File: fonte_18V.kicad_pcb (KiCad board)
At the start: 2 copper layers, 100 x 52 mm, 35 parts, among them J1 MSTBA, J2 MSTBA, J3 RJ45_Shielded, J4 RJ45_Shielded, Q1 Si2308CDS, U1 LMR16030

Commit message: temp
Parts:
- removed Ci2: 10u, Capacitor_THT:CP_Radial_D5.0mm_P2.50mm
- removed D1: MBR20200CTG, Package_TO_SOT_THT:TO-220-3_Horizontal_TabDown_SMD
- removed F1: 2A, KicadZeniteSolarLibrary18:Fuse_Holder_5x20
- removed J1, J2: MSTBA, Connector_Phoenix_MSTB:PhoenixContact_MSTBA_2,5_2-G-5,08_1x02_P5.08mm_Horizontal
- added Cie101: 10u, Capacitor_THT:CP_Radial_D5.0mm_P2.50mm, F.Cu at (60.5, 176.7)
- added D101: 4v7, Diode_SMD:D_MiniMELF, B.Cu at (47.4, 167.6)
- added D102: MBR340, Diode_SMD:D_SMA_Handsoldering, B.Cu at (93.0, 161.4)
- added D103: B1100, Diode_SMD:D_SMA_Handsoldering, F.Cu at (60.5, 160.0)
- added D104: B1100, Diode_SMD:D_SMA_Handsoldering, F.Cu at (64.0, 160.0)
- added F101: Fuse, KicadZeniteSolarLibrary18:Fuse_Holder_5x20, F.Cu at (36.1, 170.3)
- added J101: IN, TerminalBlock:TerminalBlock_bornier-3_P5.08mm, F.Cu at (32.6, 167.5)
- added J102: Conn_01x02, TerminalBlock:TerminalBlock_bornier-2_P5.08mm, F.Cu at (32.6, 156.7)
- R2: value 100 -> 1k
- moved RLed1 45.9 mm to (133.2, 168.9)
- moved Led1 45.9 mm to (136.0, 169.0)
- moved Co1 20.4 mm to (91.3, 161.6)
- moved L1 18.9 mm to (68.0, 161.3)
- moved Co3 10.8 mm to (73.8, 162.4)
- moved Co4 9.39 mm to (71.4, 162.6)
- moved Co2 9.11 mm to (85.7, 161.5)
- moved R2 0.71 mm to (45.1, 166.9)
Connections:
- net Net-(R2-Pad1) renamed /EN
- Cff1 pad 1: /CAN_18V -> /CAN_18V_DIODE
- Co1 pad 1: /CAN_18V -> /CAN_18V_DIODE
- Co2 pad 1: /CAN_18V -> /CAN_18V_DIODE
- Co3 pad 1: /CAN_18V -> /CAN_18V_DIODE
- Co4 pad 1: /CAN_18V -> /CAN_18V_DIODE
- J3 pad 1: (no net) -> Net-(J4-Pad1)
- J3 pad 2: (no net) -> Net-(J4-Pad2)
- J3 pad 9: GND -> (no net)
- J4 pad 1: (no net) -> Net-(J4-Pad1)
- J4 pad 2: (no net) -> Net-(J4-Pad2)
- J4 pad 9: GND -> (no net)
- L1 pad 2: /CAN_18V -> /CAN_18V_DIODE
- Led1 pad 2: /CAN_18V -> /CAN_18V_DIODE
- Rfbt2 pad 1: /CAN_18V -> /CAN_18V_DIODE
- U1 pad 6: (no net) -> unconnected-(U1-Pad6)
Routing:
- net /CAN_18V: track 108.7 -> 34.6 mm, vias 1 -> 0
- net Net-(CBoot1-Pad1): track 98.6 -> 34.1 mm, vias 1 -> 0
- net /CAN_18V_DIODE: track 0.00 -> 43.1 mm
- net Net-(J4-Pad1): track 0.00 -> 30.4 mm, vias 0 -> 1
- net Net-(J4-Pad2): track 0.00 -> 27.6 mm
- net GND: track 167.3 -> 147.9 mm, vias 4 -> 3
- net Net-(J101-Pad2): track 0.00 -> 9.50 mm
- net Net-(F1-Pad2): track 9.50 -> 0.00 mm
- net Net-(Cie101-Pad1): track 62.8 -> 58.2 mm

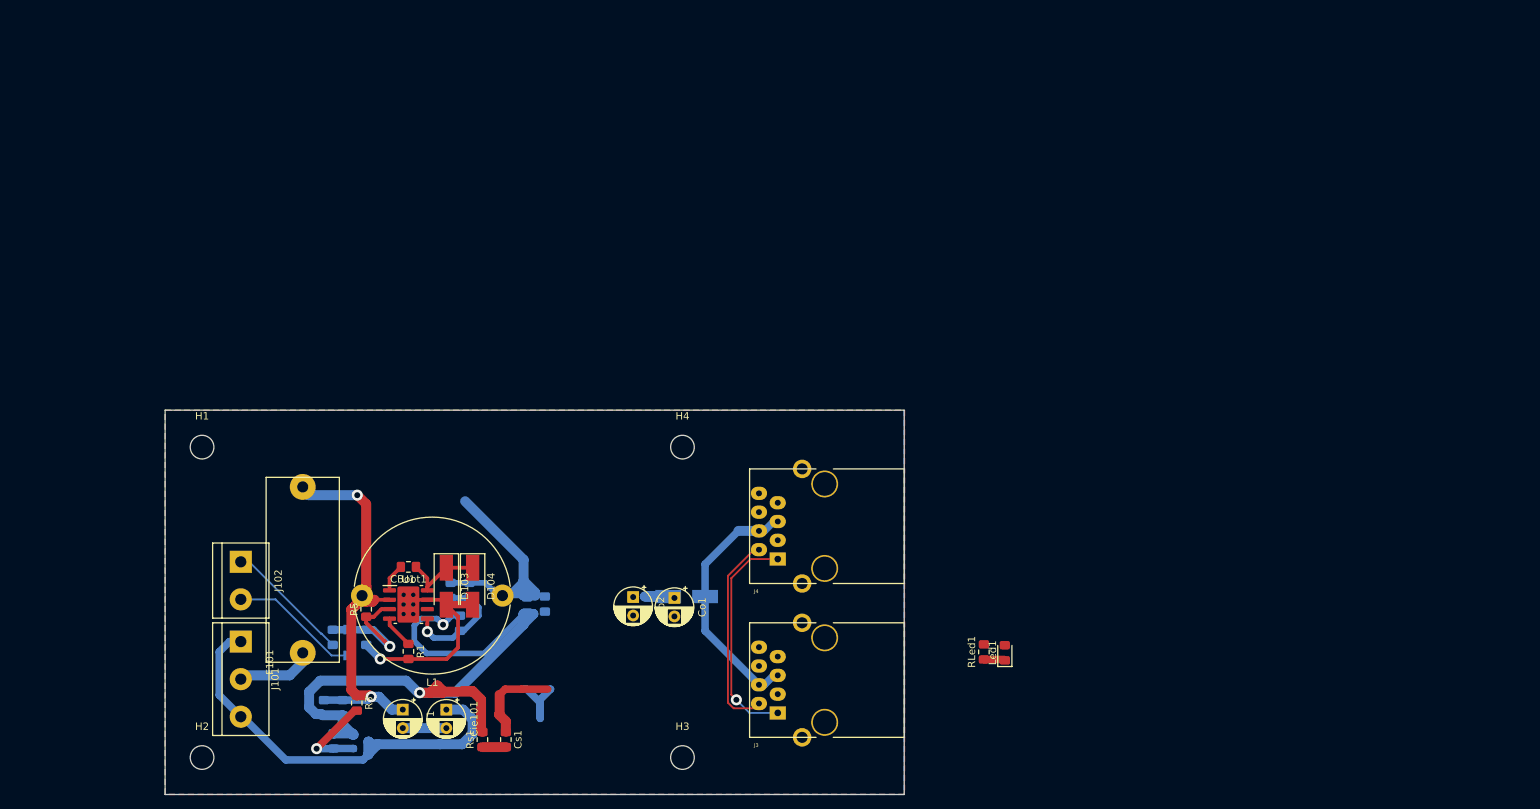
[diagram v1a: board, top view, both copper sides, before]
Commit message: Duplicate fonts for redundancy and initialized layout
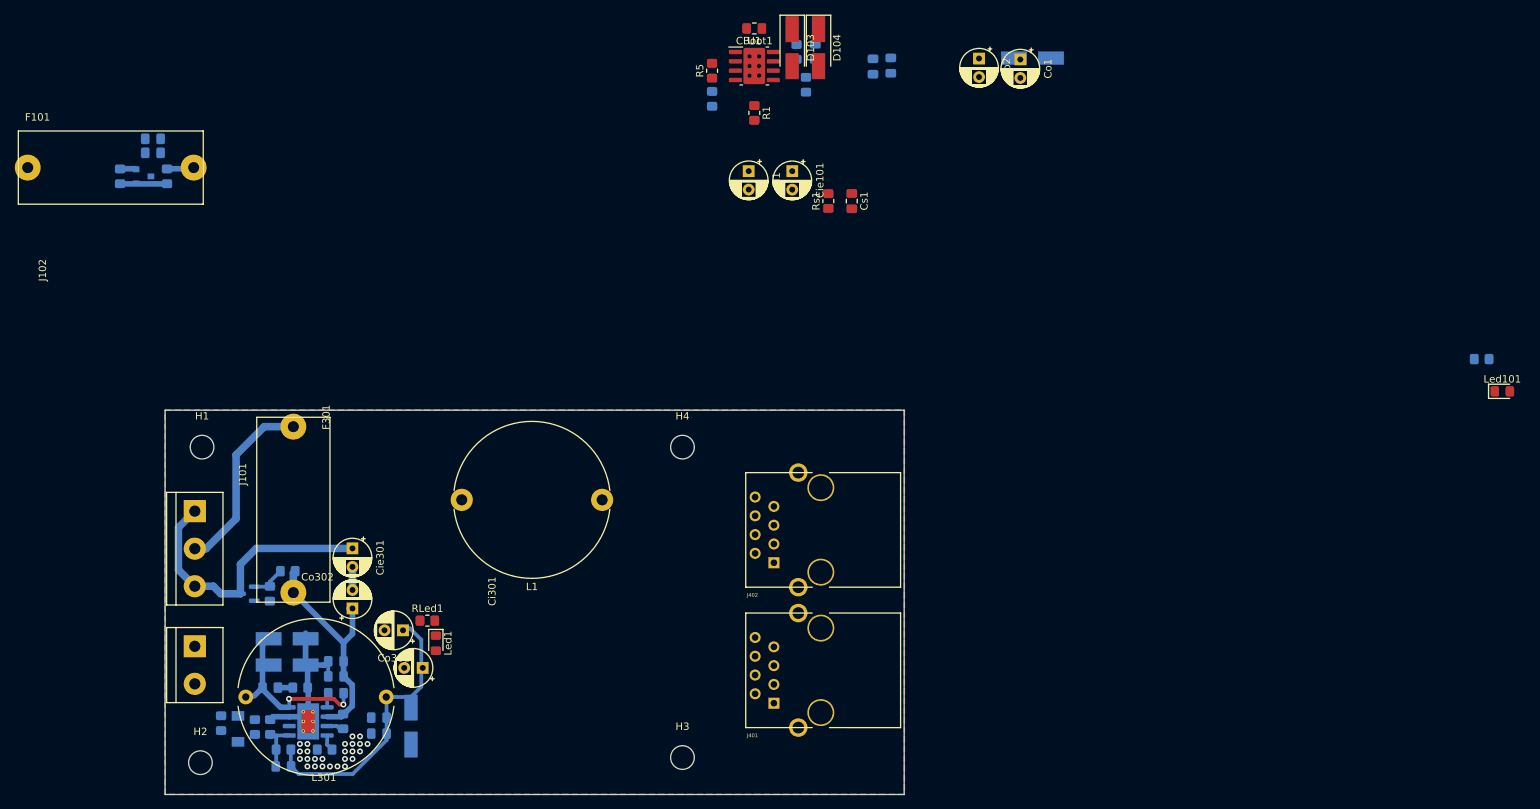
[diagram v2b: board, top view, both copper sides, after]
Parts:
- removed J3, J4: RJ45_Shielded, MFP19RJ45:RJ45_YH59_01
- added CBoot301: 100nF, Capacitor_SMD:C_0805_2012Metric_Pad1.18x1.45mm_HandSolder, B.Cu at (45.5, 174.5)
- added Cff301: na, Capacitor_SMD:C_0805_2012Metric_Pad1.18x1.45mm_HandSolder, B.Cu at (38.4, 184.4)
- added Ci301: 10u, Capacitor_THT:CP_Radial_D5.0mm_P2.50mm, F.Cu at (47.8, 163.0)
- added Cie301: 10u, Capacitor_THT:CP_Radial_D5.0mm_P2.50mm, F.Cu at (47.8, 154.9)
- added Cin301: 100nF, Capacitor_SMD:C_0805_2012Metric_Pad1.18x1.45mm_HandSolder, B.Cu at (45.5, 170.2)
- added Cin302: 100nF, Capacitor_SMD:C_0805_2012Metric_Pad1.18x1.45mm_HandSolder, B.Cu at (45.5, 172.2)
- added Co301: 47u, Capacitor_THT:CP_Radial_D5.0mm_P2.50mm, F.Cu at (54.6, 166.0)
- added Co302: 47u, Capacitor_THT:CP_Radial_D5.0mm_P2.50mm, F.Cu at (57.3, 171.1)
- added Co303: o.1u, Capacitor_SMD:C_0805_2012Metric_Pad1.18x1.45mm_HandSolder, B.Cu at (51.3, 177.8)
- added Co304: 0.1u, Capacitor_SMD:C_0805_2012Metric_Pad1.18x1.45mm_HandSolder, B.Cu at (51.3, 180.0)
- added Cs301: 100n, Capacitor_SMD:C_0805_2012Metric_Pad1.18x1.45mm_HandSolder, B.Cu at (36.6, 173.7)
- added D301: B1100, Diode_SMD:D_SMA_Handsoldering, B.Cu at (38.9, 167.1)
- added D302: B1100, Diode_SMD:D_SMA_Handsoldering, B.Cu at (38.9, 170.7)
- added D303: MBR340, Diode_SMD:D_SMA_Handsoldering, B.Cu at (55.7, 178.9)
- added F301: Fuse, KicadZeniteSolarLibrary18:Fuse_Holder_5x20, F.Cu at (44.7, 137.2)
- added J401: RJ45_Shielded, MFP19RJ45:RJ45_YH59_01, F.Cu at (104.8, 175.8)
- added J402: RJ45_Shielded, MFP19RJ45:RJ45_YH59_01, F.Cu at (104.8, 156.8)
- added L301: 100uH, Inductor_THT:L_Radial_D21.0mm_P19.00mm, F.Cu at (33.3, 175.0)
- added Led101: LED, LED_SMD:LED_0805_2012Metric_Pad1.15x1.40mm_HandSolder, F.Cu at (203.3, 133.6)
- added Q301: Si2308CDS, Package_TO_SOT_SMD:SOT-23, B.Cu at (33.5, 161.0)
- added R301: 220K, Resistor_SMD:R_0805_2012Metric_Pad1.20x1.40mm_HandSolder, B.Cu at (39.0, 158.0)
- added R302: 100K, Resistor_SMD:R_0805_2012Metric_Pad1.20x1.40mm_HandSolder, B.Cu at (36.6, 161.0)
- added R303: 10K, Resistor_SMD:R_0805_2012Metric_Pad1.20x1.40mm_HandSolder, B.Cu at (46.5, 178.3)
- added R304: NA, Resistor_SMD:R_0805_2012Metric_Pad1.20x1.40mm_HandSolder, B.Cu at (34.5, 179.1)
- added R305: 47k, Resistor_SMD:R_0805_2012Metric_Pad1.20x1.40mm_HandSolder, B.Cu at (44.0, 182.1)
- added RLed101: 1k5, Resistor_SMD:R_0805_2012Metric_Pad1.20x1.40mm_HandSolder, B.Cu at (200.5, 129.3)
- added Rfbb301: 8k2, Resistor_SMD:R_0805_2012Metric_Pad1.20x1.40mm_HandSolder, B.Cu at (36.6, 179.1)
- added Rfbt301: 230k, Resistor_SMD:R_0805_2012Metric_Pad1.20x1.40mm_HandSolder, B.Cu at (38.4, 182.1)
- added Rs301: 2k2, Resistor_SMD:R_0805_2012Metric_Pad1.20x1.40mm_HandSolder, B.Cu at (40.7, 173.7)
- added U301: LMR16030, Package_SO:Texas_R-PDSO-G8_EP2.95x4.9mm_Mask2.4x3.1mm_ThermalVias, B.Cu at (41.8, 178.3)
- CBoot1, Cff1, Cin2, Cin3, Co3, Co4, Cs1: footprint Capacitor_SMD:C_0805_2012Metric_Pad1.15x1.40mm_HandSolder -> Capacitor_SMD:C_0805_2012Metric_Pad1.18x1.45mm_HandSolder
- R1, R2, R4, R5, R6, RLed1, Rfbb1, Rfbt2, Rs1: footprint Resistor_SMD:R_0805_2012Metric_Pad1.15x1.40mm_HandSolder -> Resistor_SMD:R_0805_2012Metric_Pad1.20x1.40mm_HandSolder
- R3: footprint Resistor_SMD:R_0805_2012Metric_Pad1.15x1.40mm_HandSolder -> Resistor_SMD:R_0805_2012Metric_Pad1.20x1.40mm_HandSolder; moved to B.Cu
- moved Cff1 86.6 mm to (110.4, 87.7)
- moved Ci1 86.6 mm to (101.4, 103.9)
- moved Cie101 86.6 mm to (107.3, 103.9)
- moved Co1 86.6 mm to (138.1, 88.8)
- moved Co2 86.6 mm to (132.5, 88.6)
- moved Co4 86.6 mm to (118.2, 89.7)
- moved D102 86.6 mm to (139.8, 88.6)
- moved D103 86.6 mm to (107.3, 87.2)
- moved D104 86.6 mm to (110.8, 87.2)
- moved R1 86.6 mm to (102.1, 96.0)
- moved R5 86.6 mm to (96.4, 90.3)
- moved R6 86.6 mm to (96.4, 94.1)
- moved Rfbb1 86.6 mm to (109.1, 92.2)
- moved Rfbt2 86.6 mm to (107.8, 87.7)
- moved U1 86.6 mm to (102.1, 89.6)
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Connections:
- net /Feedback renamed /supply1/Feedback
- net /snbr renamed /supply1/snbr
- net Net-(Cie101-Pad1) renamed /supply1/GND_IN
- net Net-(J101-Pad2) renamed /supply1/IN
- Cff1 pad 1: /CAN_18V_DIODE -> /supply1/CAN_18V_DIODE
- Co1 pad 1: /CAN_18V_DIODE -> /supply1/CAN_18V_DIODE
- Co2 pad 1: /CAN_18V_DIODE -> /supply1/CAN_18V_DIODE
- Co3 pad 1: /CAN_18V_DIODE -> /supply1/CAN_18V_DIODE
- Co4 pad 1: /CAN_18V_DIODE -> /supply1/CAN_18V_DIODE
- D102 pad 1: /CAN_18V -> /CAN/CAN_18V
- D102 pad 2: /CAN_18V_DIODE -> /supply1/CAN_18V_DIODE
- L1 pad 2: /CAN_18V_DIODE -> /supply1/CAN_18V_DIODE
- Led1 pad 2: /CAN_18V_DIODE -> /CAN/CAN_18V
- Rfbt2 pad 1: /CAN_18V_DIODE -> /supply1/CAN_18V_DIODE
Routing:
- net GND: track 147.9 -> 23.7 mm, vias 3 -> 25
- net Net-(Ci1-Pad1): track 61.3 -> 3.45 mm, vias 2 -> 0
- net /CAN_18V_DIODE: track 43.1 -> 0.00 mm
- net /supply2/CAN_18V_DIODE: track 0.00 -> 37.8 mm
- net /CAN_18V: track 34.6 -> 0.00 mm
- net Net-(CBoot1-Pad1): track 34.1 -> 0.00 mm
- net Net-(Ci301-Pad1): track 0.00 -> 31.3 mm
- net Net-(J4-Pad1): track 30.4 -> 0.00 mm, vias 1 -> 0
- net Net-(J4-Pad2): track 27.6 -> 0.00 mm
- net Net-(CBoot301-Pad1): track 0.00 -> 23.6 mm, vias 0 -> 2
- net /supply1/GND_IN: track 58.2 -> 40.1 mm
- net Net-(R2-Pad2): track 17.2 -> 0.00 mm
- net /supply1/Feedback: track 15.8 -> 0.00 mm, vias 1 -> 0
- net /supply1/IN: track 9.50 -> 25.2 mm
- net /EN: track 16.9 -> 2.31 mm, vias 1 -> 0
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
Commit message: almost finished
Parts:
- added D201: MBR340, Diode_SMD:D_SMA_Handsoldering, B.Cu at (85.8, 154.0)
- added D304: MBR340, Diode_SMD:D_SMA_Handsoldering, B.Cu at (85.9, 178.1)
- CBoot1, Cs1, D103, D104, R1, R5, Rs1, U1: moved to B.Cu
- D101, R2, RLed101: moved to F.Cu
- J401, J402: footprint MFP19RJ45:RJ45_YH59_01 -> KicadZeniteSolarLibrary18:RJ45_YH59_01
- moved Led101 128.1 mm to (82.3, 175.5), turned to -90 degrees
- moved RLed101 124.0 mm to (84.6, 173.4), turned to 90 degrees
- moved D102 87.3 mm to (82.0, 154.0), turned to 90 degrees
- moved D104 82.0 mm to (65.4, 155.4), turned to 90 degrees
- moved D103 82.0 mm to (61.8, 155.4), turned to 90 degrees
- moved Co1 80.3 mm to (82.0, 146.2), turned to 90 degrees
- moved Co2 75.8 mm to (78.5, 141.8), turned to 90 degrees
- moved Cff1 75.0 mm to (79.1, 155.9)
- moved Rfbt2 74.9 mm to (76.8, 155.9)
- moved Rfbb1 74.5 mm to (73.8, 157.7), turned to 180 degrees
- moved Cie101 72.3 mm to (49.0, 146.6), turned to 0 degrees
- moved CBoot1 72.2 mm to (69.2, 148.8), turned to -90 degrees
- moved Co3 71.9 mm to (72.5, 143.0)
- moved U1 69.3 mm to (73.0, 152.6), turned to -90 degrees
- moved Co4 68.8 mm to (74.7, 143.0)
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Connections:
- D303 pad 1: /supply2/CAN_18V -> /CAN/CAN_18V
- Led1 pad 2: /CAN/CAN_18V -> /supply1/CAN_18V_DIODE
- Led101 pad 2: /supply2/CAN_18V -> /supply2/CAN_18V_DIODE
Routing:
- net GND: track 23.7 -> 291.8 mm, vias 25 -> 151
- net /EN: track 2.31 -> 97.4 mm, vias 0 -> 4
- net /supply1/GND_IN: track 40.1 -> 99.1 mm
- net /CAN/CAN_18V: track 0.00 -> 50.2 mm
- net /supply1/CAN_18V_DIODE: track 0.00 -> 35.1 mm, vias 0 -> 2
- net Net-(J401-Pad2): track 0.00 -> 28.9 mm
- net Net-(Ci1-Pad1): track 3.45 -> 31.5 mm
- net Net-(CBoot1-Pad1): track 0.00 -> 23.6 mm, vias 0 -> 2
- net Net-(J401-Pad1): track 0.00 -> 20.3 mm
- net Net-(J102-Pad1): track 0.00 -> 8.33 mm
- net /supply1/Feedback: track 0.00 -> 6.57 mm
- net /supply1/IN: track 25.2 -> 31.1 mm
- net Net-(Ci1-Pad2): track 0.00 -> 3.77 mm
- net /supply2/CAN_18V_DIODE: track 37.8 -> 35.1 mm, vias 0 -> 1
- net Net-(Led101-Pad1): track 0.00 -> 2.34 mm
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
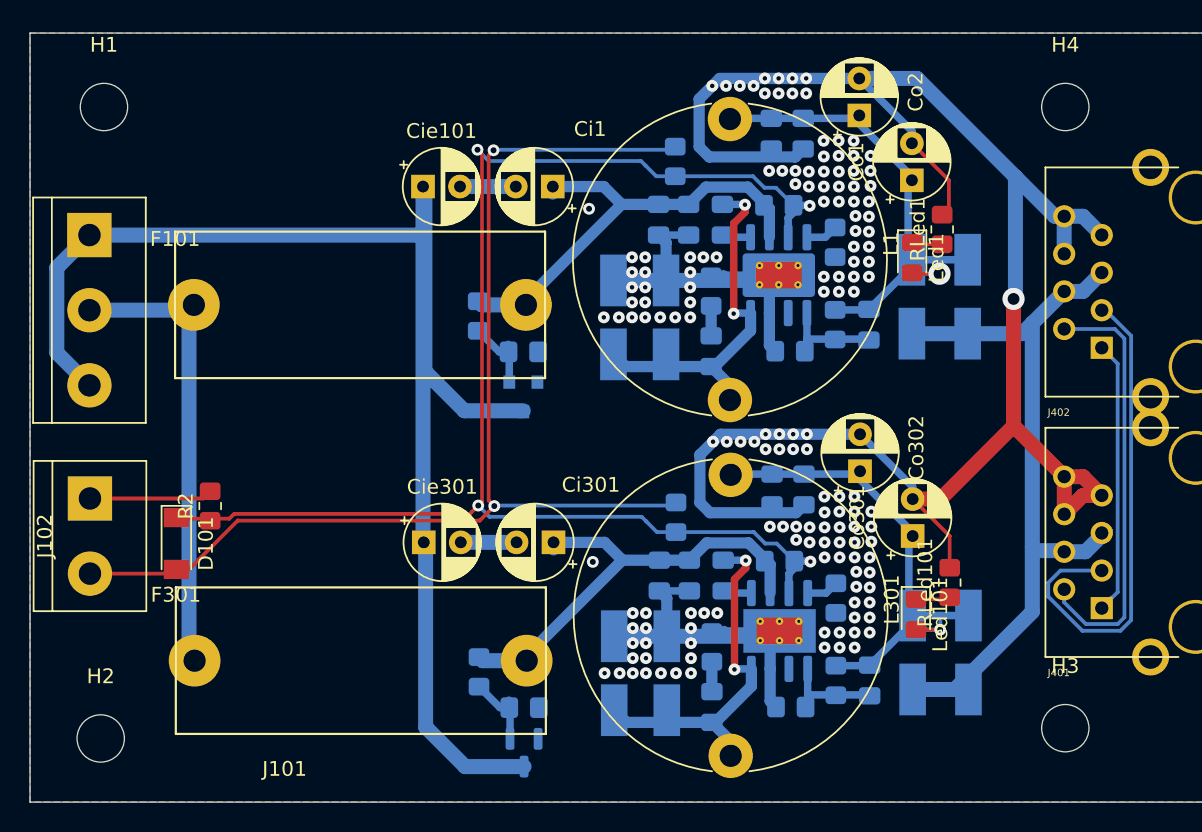
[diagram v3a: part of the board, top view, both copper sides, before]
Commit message: run DRC and turn invisible reference designators
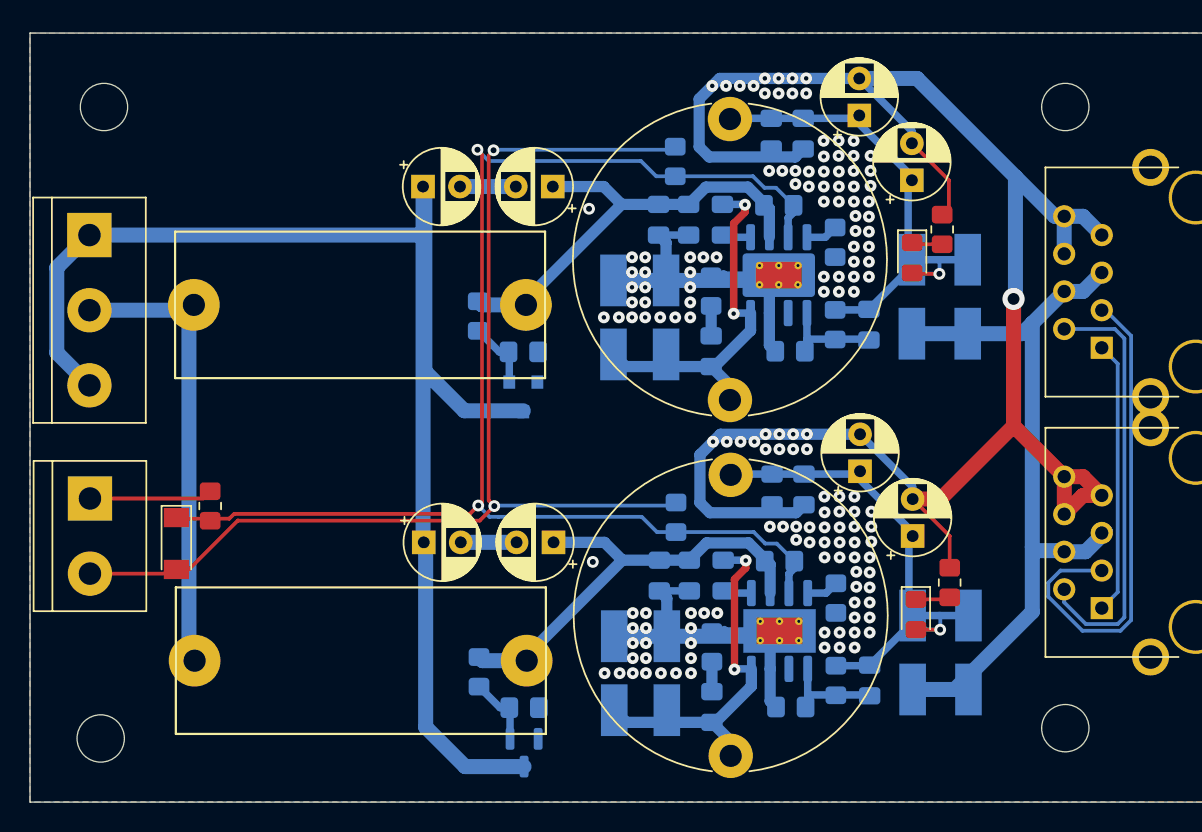
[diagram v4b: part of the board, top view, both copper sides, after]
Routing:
- net /EN: track 97.4 -> 95.0 mm, vias 4 -> 2
- net GND: track 291.8 -> 289.5 mm
- net Net-(J401-Pad1): track 20.3 -> 18.5 mm
- net /supply1/IN: track 31.1 -> 30.0 mm
- net Net-(Ci1-Pad1): track 31.5 -> 30.6 mm
- net Net-(Ci301-Pad1): track 31.5 -> 30.6 mm
- net /supply2/CAN_18V_DIODE: track 35.1 -> 34.3 mm
- net /supply1/CAN_18V_DIODE: track 35.1 -> 34.3 mm, vias 2 -> 1
- net Net-(Q301-Pad1): track 5.28 -> 4.70 mm
- net Net-(Q1-Pad1): track 5.28 -> 4.70 mm
- net /supply1/GND_IN: track 99.1 -> 98.6 mm

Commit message: Add silkscreen for connectors and author label
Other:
- board size 100 x 52 mm -> 90 x 52 mm
- board text added: "3A"
- board text added: "GND | IN | GND"
- board text added: "GND|EN"
- board text added: "SUPPLY 1 ON"
- board text added: "SUPPLY 2 ON"
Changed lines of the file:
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@@
       (effects (font (size 1 1) (thickness 0.15)) (justify mirror))
     )
-    (fp_text value "MBR340" (at 0 -2.6 90) (layer "B.Fab")
+    (fp_text value "MBR340" (at 5.6185 0 90) (layer "B.Fab")
       (effects (font (size 1 1) (thickness 0.15)) (justify mirror))
     )
@@
       (effects (font (size 1 1) (thickness 0.15)) (justify mirror))
     )
-    (fp_text value "MBR340" (at 0 -2.6 90) (layer "B.Fab")
+    (fp_text value "MBR340" (at 5.6185 -0.0355 90) (layer "B.Fab")
       (effects (font (size 1 1) (thickness 0.15)) (justify mirror))
     )
@@
       (effects (font (size 1 1) (thickness 0.15)) (justify mirror))
     )
-    (fp_text value "230k" (at 0 -1.65 -270) (layer "B.Fab")
+    (fp_text value "230k" (at 3.919888 -0.0755 -270) (layer "B.Fab")
       (effects (font (size 1 1) (thickness 0.15)) (justify mirror))
     )
@@
   )
   (gr_line (start 22.4 188.2) (end 22.4 136.2) (layer "Edge.Cuts") (width 0.05))
-  (gr_line (start 122.4 188.2) (end 22.4 188.2) (layer "Edge.Cuts") (width 0.05))
-  (gr_line (start 122.4 136.2) (end 122.4 188.2) (layer "Edge.Cuts") (width 0.05))
-  (gr_line (start 22.4 136.2) (end 122.4 136.2) (layer "Edge.Cuts") (width 0.05))
+  (gr_line (start 112.395 188.2) (end 22.4 188.2) (layer "Edge.Cuts") (width 0.05))
+  (gr_line (start 112.395 136.2) (end 112.395 188.2) (layer "Edge.Cuts") (width 0.05))
+  (gr_line (start 22.4 136.2) (end 112.395 136.2) (layer "Edge.Cuts") (width 0.05))
+  (gr_text "GND | IN | GND" (at 31.242 155.194 90) (layer "B.SilkS")
+    (effects (font (size 1 1) (thickness 0.15)))
+  )
+  (gr_text "GND|EN" (at 23.622 178.816 90) (layer "B.SilkS")
+    (effects (font (size 1 1) (thickness 0.15)))
+  )
+  (gr_text "SUPPLY 1 ON" (at 86.36 175.26 90) (layer "F.SilkS")
+    (effects (font (size 1 1) (thickness 0.15)))
+  )
+  (gr_text "GND | IN | GND" (at 31.242 155.194 90) (layer "F.SilkS")
+    (effects (font (size 1 1) (thickness 0.15)))
+  )
+  (gr_text "GND|EN" (at 23.622 178.816 90) (layer "F.SilkS")
+    (effects (font (size 1 1) (thickness 0.15)))
+  )
+  (gr_text "3A" (at 56.515 184.785) (layer "F.SilkS")
+    (effects (font (size 1 1) (thickness 0.15)))
+  )
+  (gr_text "SUPPLY 2 ON" (at 86.36 150.495 90) (layer "F.SilkS")
+    (effects (font (size 1 1) (thickness 0.15)))
+  )
+  (gr_text "3A" (at 56.515 160.655) (layer "F.SilkS")
+    (effects (font (size 1 1) (thickness 0.15)))
+  )
   (segment (start 69.553612 150.007888) (end 71.12 150.007888) (width 0.508) (layer "B.Cu") (net 1))
   (segment (start 70.739 148.3145) (end 69.977 149.0765) (width 0.508) (layer "F.Cu") (net 2))
@@
       (pts
         (xy 22.4 136.2)
-        (xy 122.45 136.19)
-        (xy 122.45 188.19)
+        (xy 112.29 136.19)
+        (xy 112.29 188.19)
         (xy 22.4 188.2)
       )
@@
       (pts
         (xy 22.4 136.21875)
-        (xy 122.4 136.2)
-        (xy 122.41 188.19)
+        (xy 112.235852 136.201956)
+        (xy 112.245852 188.191956)
         (xy 22.4 188.18125)
       )
